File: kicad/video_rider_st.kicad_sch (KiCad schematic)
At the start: 32 parts, among them J1 F3311A7H121020E200, J2 F3311A7H121020E200, J3 Conn_01x02_Male, J4 Conn_01x03_Male, J5 F3311A7H121020E200, J6 F3311A7H121020E200, J7 Conn_01x06_Male, U1 ST_SHIFTER_PHY, U10 ST_GLUE_SOCKET, U2 ST_SHIFTER_SOCKET, U3 Pico, U4 74HC245, U5 74HC245, U6 74HC245, U7 74HC245, U8 XC95144XL-TQ100, U9 ST_GLUE_PHY, X1 CXO_DIP14

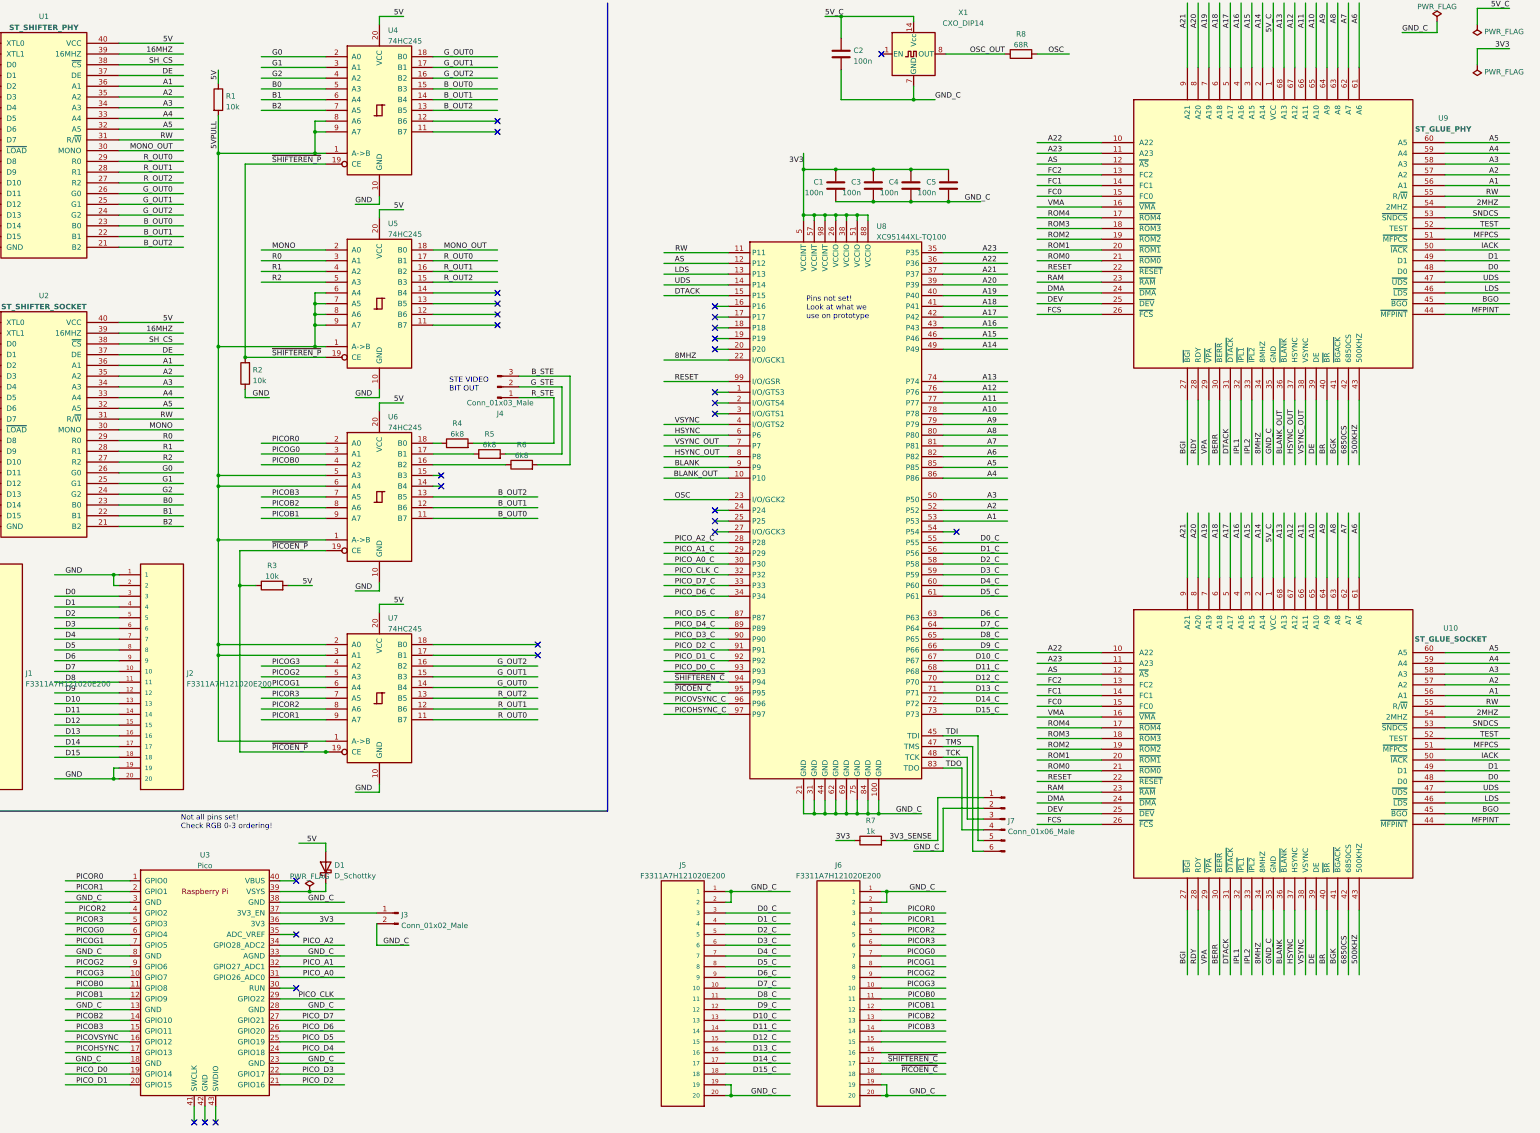
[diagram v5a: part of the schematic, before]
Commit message: Basic board outline and routeing done. Need sanity and DRC check
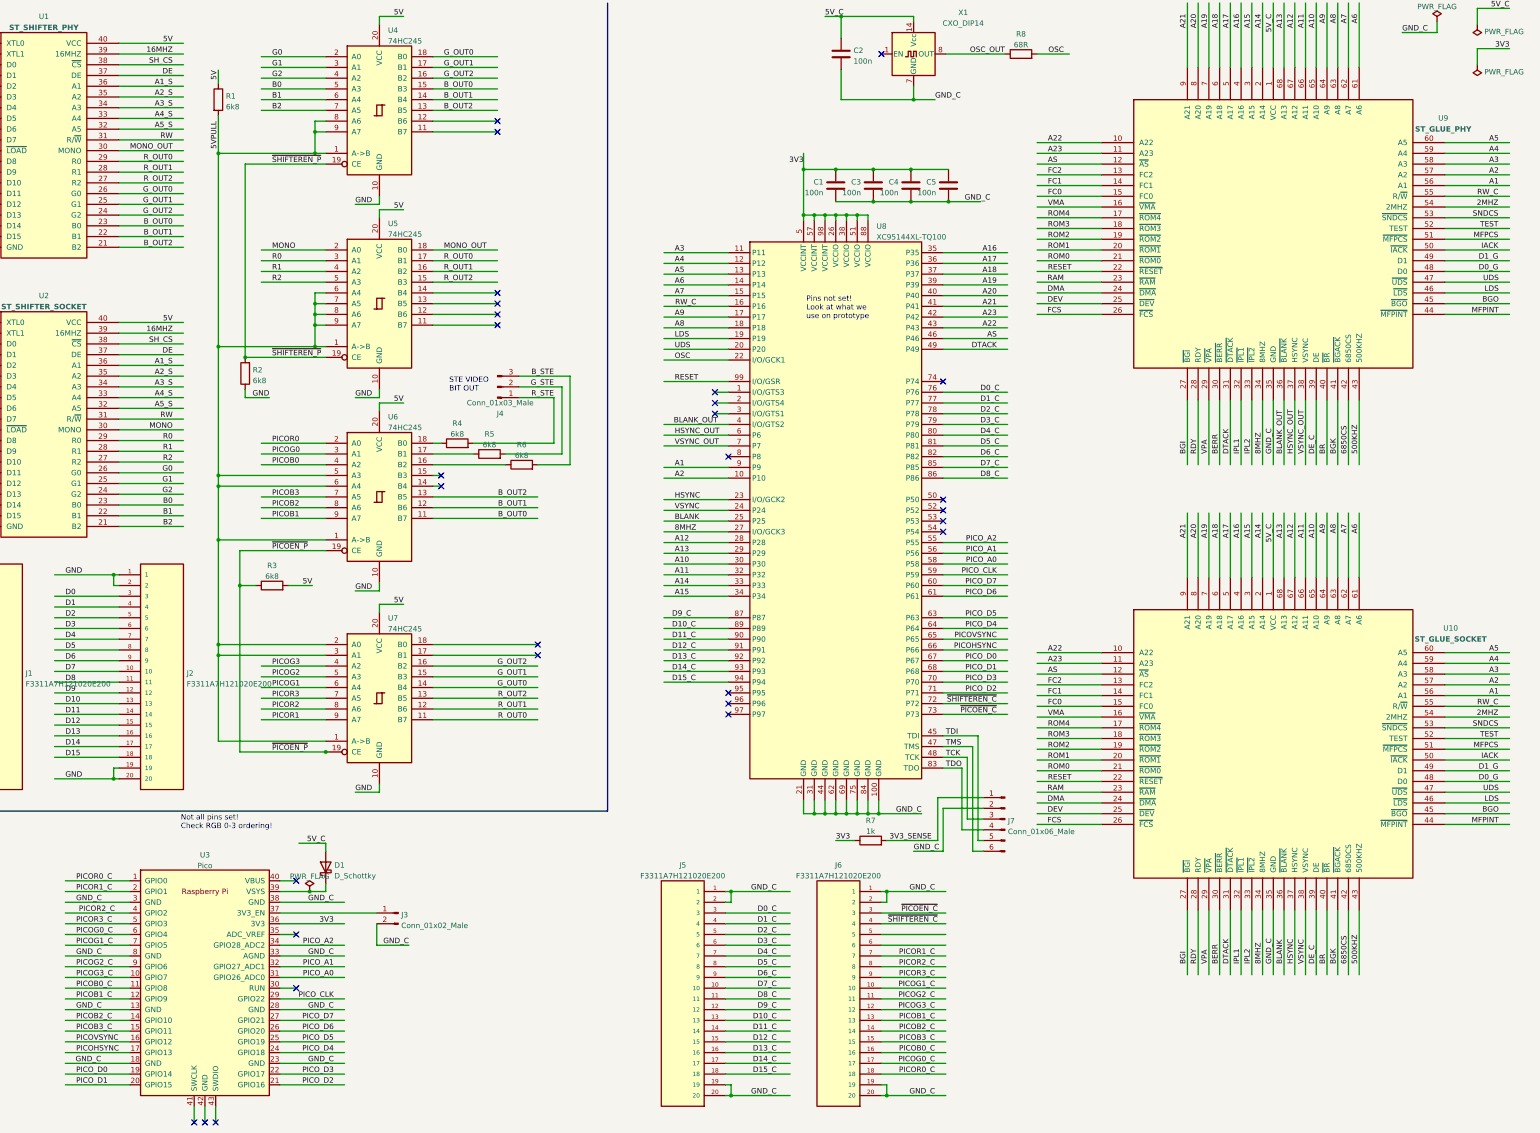
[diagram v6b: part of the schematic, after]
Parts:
- J3: footprint Connector_PinHeader_2.54mm:PinHeader_1x02_P2.54mm_Vertical -> Connector_PinHeader_2.54mm:PinHeader_1x02_P2.54mm_Horizontal
- J4: footprint Connector_PinHeader_2.54mm:PinHeader_1x03_P2.54mm_Horizontal -> Connector_PinHeader_2.54mm:PinHeader_1x03_P2.54mm_Vertical
- J7: footprint Connector_PinHeader_2.54mm:PinHeader_1x06_P2.54mm_Horizontal -> Connector_PinHeader_2.54mm:PinHeader_1x06_P2.54mm_Vertical
- R1, R2, R3: value 10k -> 6k8
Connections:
- net PICO_A0_C is gone; now on net A10: U8.30 (P30)
- net PICO_A1_C is gone; now on net A13: U8.29 (P29)
- net PICO_A2_C is gone; now on net A12: U8.28 (P28)
- net PICO_CLK_C is gone; now on net A11: U8.32 (P32)
- net PICO_D0_C is gone; now on net D14_C: U8.93 (P93)
- net PICO_D1_C is gone; now on net D13_C: U8.92 (P92)
- net PICO_D2_C is gone; now on net D12_C: U8.91 (P91)
- net PICO_D3_C is gone; now on net D11_C: U8.90 (P90)
- net PICO_D4_C is gone; now on net D10_C: U8.89 (P89)
- net PICO_D5_C is gone; now on net D9_C: U8.87 (P87)
- net PICO_D6_C is gone; now on net A15: U8.34 (P34)
- net PICO_D7_C is gone; now on net A14: U8.33 (P33)
- net 5V: no longer D1.2 (A)
- net 5V_C: now also D1.2 (A)
- net 8MHZ: now also U8.27 (I/O/GCK3); no longer U8.22 (I/O/GCK1)
- net A1: now also U8.9 (P9); no longer U1.36 (A1), U2.36 (A1), U8.53 (P53)
- net A10: no longer U8.78 (P78)
- net A11: no longer U8.77 (P77)
- net A12: no longer U8.76 (P76)
- net A13: no longer U8.74 (P74)
- net A14: no longer U8.49 (P49)
- net A15: no longer U8.46 (P46)
- net A16: now also U8.35 (P35); no longer U8.43 (P43)
- net A17: now also U8.36 (P36); no longer U8.42 (P42)
- net A18: now also U8.37 (P37); no longer U8.41 (P41)
- net A19: now also U8.39 (P39); no longer U8.40 (P40)
- net A2: now also U8.10 (P10); no longer U1.35 (A2), U2.35 (A2), U8.52 (P52)
- net A20: now also U8.40 (P40); no longer U8.39 (P39)
- net A21: now also U8.41 (P41); no longer U8.37 (P37)
- net A22: now also U8.43 (P43); no longer U8.36 (P36)
- net A23: now also U8.42 (P42); no longer U8.35 (P35)
- net A3: now also U8.11 (P11); no longer U1.34 (A3), U2.34 (A3), U8.50 (P50)
- net A4: now also U8.12 (P12); no longer U1.33 (A4), U2.33 (A4), U8.86 (P86)
- net A5: now also U8.13 (P13); no longer U1.32 (A5), U2.32 (A5), U8.85 (P85)
- net A6: now also U8.14 (P14); no longer U8.82 (P82)
- net A7: now also U8.15 (P15); no longer U8.81 (P81)
- net A8: now also U8.18 (P18); no longer U8.80 (P80)
- net A9: now also U8.17 (P17); no longer U8.79 (P79)
- net AS: now also U8.46 (P46); no longer U8.12 (P12)
- net BLANK: now also U8.25 (P25); no longer U8.9 (P9)
- net BLANK_OUT: now also U8.4 (I/O/GTS2); no longer U8.10 (P10)
- net D0: no longer U10.48 (D0), U9.48 (D0)
- net D0_C: now also U8.76 (P76); no longer U8.55 (P55)
- net D1: no longer U10.49 (D1), U9.49 (D1)
- net D10_C: no longer U8.67 (P67)
- net D11_C: no longer U8.68 (P68)
- net D12_C: no longer U8.70 (P70)
- net D13_C: no longer U8.71 (P71)
- net D14_C: no longer U8.72 (P72)
- net D15_C: now also U8.94 (P94); no longer U8.73 (P73)
- net D1_C: now also U8.77 (P77); no longer U8.56 (P56)
- net D2_C: now also U8.78 (P78); no longer U8.58 (P58)
- net D3_C: now also U8.79 (P79); no longer U8.59 (P59)
- net D4_C: now also U8.80 (P80); no longer U8.60 (P60)
- net D5_C: now also U8.81 (P81); no longer U8.61 (P61)
- net D6_C: now also U8.82 (P82); no longer U8.63 (P63)
- net D7_C: now also U8.85 (P85); no longer U8.64 (P64)
- net D8_C: now also U8.86 (P86); no longer U8.65 (P65)
- net D9_C: no longer U8.66 (P66)
- net DE: no longer U10.39 (DE), U9.39 (DE)
- net DTACK: now also U8.49 (P49); no longer U8.15 (P15)
- net HSYNC: now also U8.23 (I/O/GCK2); no longer U8.6 (P6)
- net HSYNC_OUT: now also U8.6 (P6); no longer U8.8 (P8)
- net LDS: now also U8.19 (P19); no longer U8.13 (P13)
- net OSC: now also U8.22 (I/O/GCK1); no longer U8.23 (I/O/GCK2)
- net PICOB0: no longer J6.11, U3.11 (GPIO8)
- net PICOB1: no longer J6.12, U3.12 (GPIO9)
- net PICOB2: no longer J6.13, U3.14 (GPIO10)
- net PICOB3: no longer J6.14, U3.15 (GPIO11)
- net PICOG0: no longer J6.7, U3.6 (GPIO4)
- net PICOG1: no longer J6.8, U3.7 (GPIO5)
- net PICOG2: no longer J6.9, U3.9 (GPIO6)
- net PICOG3: no longer J6.10, U3.10 (GPIO7)
- net PICOHSYNC: now also U8.66 (P66)
- net PICOR0: no longer J6.3, U3.1 (GPIO0)
- net PICOR1: no longer J6.4, U3.2 (GPIO1)
- net PICOR2: no longer J6.5, U3.4 (GPIO2)
- net PICOR3: no longer J6.6, U3.5 (GPIO3)
- net PICOVSYNC: now also U8.65 (P65)
- net PICO_A0: now also U8.58 (P58)
- net PICO_A1: now also U8.56 (P56)
- net PICO_A2: now also U8.55 (P55)
- net PICO_CLK: now also U8.59 (P59)
- net PICO_D0: now also U8.67 (P67)
- net PICO_D1: now also U8.68 (P68)
- net PICO_D2: now also U8.71 (P71)
- net PICO_D3: now also U8.70 (P70)
- net PICO_D4: now also U8.64 (P64)
- net PICO_D5: now also U8.63 (P63)
- net PICO_D6: now also U8.61 (P61)
- net PICO_D7: now also U8.60 (P60)
- net RW: no longer U10.55 (R/~{W}), U8.11 (P11), U9.55 (R/~{W})
- net UDS: now also U8.20 (P20); no longer U8.14 (P14)
- net VSYNC: now also U8.24 (P24); no longer U8.4 (I/O/GTS2)
- net ~{PICOEN_C}: now also J6.3, U8.73 (P73); no longer J6.18, U8.95 (P95)
- net ~{SHIFTEREN_C}: now also J6.4, U8.72 (P72); no longer J6.17, U8.94 (P94)
- net RW_C: now reaches U8.16 (P16)
- net RW_C: now also U10.55 (R/~{W}), U9.55 (R/~{W})
- net PICOB3_C: now reaches J6.15
- net PICOB3_C: now also U3.15 (GPIO11)
- net PICOB0_C: now reaches J6.16
- net PICOB0_C: now also U3.11 (GPIO8)
- net PICOHSYNC_C: no longer names the net of U8.97 (P97)
- net PICOVSYNC_C: no longer names the net of U8.96 (P96)
- new net A1_S: U1.36 (A1), U2.36 (A1)
- new net A2_S: U1.35 (A2), U2.35 (A2)
- new net A3_S: U1.34 (A3), U2.34 (A3)
- new net A4_S: U1.33 (A4), U2.33 (A4)
- new net A5_S: U1.32 (A5), U2.32 (A5)
- new net D0_G: U10.48 (D0), U9.48 (D0)
- new net D1_G: U10.49 (D1), U9.49 (D1)
- new net DE_C: U10.39 (DE), U9.39 (DE)
- new net PICOB1_C: J6.13, U3.12 (GPIO9)
- new net PICOB2_C: J6.14, U3.14 (GPIO10)
- new net PICOG0_C: J6.17, U3.6 (GPIO4)
- new net PICOG1_C: J6.10, U3.7 (GPIO5)
- new net PICOG2_C: J6.11, U3.9 (GPIO6)
- new net PICOG3_C: J6.12, U3.10 (GPIO7)
- new net PICOR0_C: J6.18, U3.1 (GPIO0)
- new net PICOR1_C: J6.7, U3.2 (GPIO1)
- new net PICOR2_C: J6.8, U3.4 (GPIO2)
- new net PICOR3_C: J6.9, U3.5 (GPIO3)

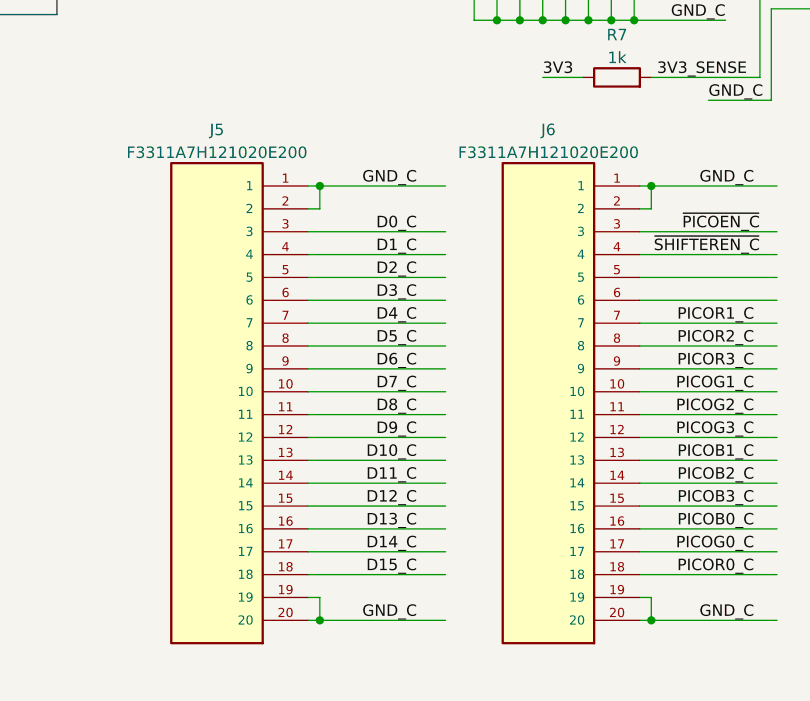
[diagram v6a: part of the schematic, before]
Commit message: Rerouteing pico to bottom layer
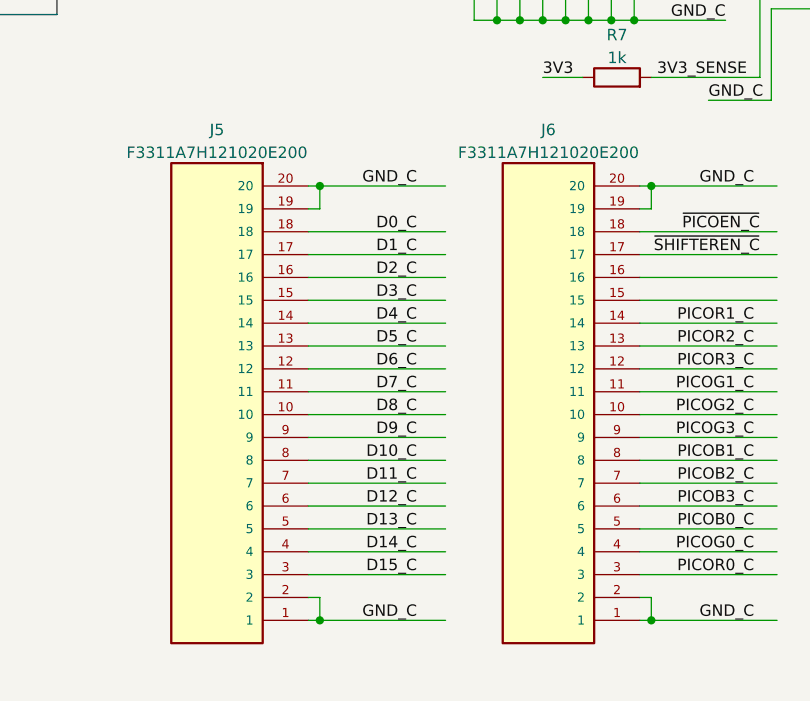
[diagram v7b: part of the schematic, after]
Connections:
- net D0_C: now also J5.18; no longer J5.3
- net D10_C: now also J5.8; no longer J5.13
- net D11_C: now also J5.7; no longer J5.14
- net D12_C: now also J5.6; no longer J5.15
- net D13_C: now also J5.5; no longer J5.16
- net D14_C: now also J5.4; no longer J5.17
- net D15_C: now also J5.3; no longer J5.18
- net D1_C: now also J5.17; no longer J5.4
- net D2_C: now also J5.16; no longer J5.5
- net D3_C: now also J5.15; no longer J5.6
- net D4_C: now also J5.14; no longer J5.7
- net D5_C: now also J5.13; no longer J5.8
- net D6_C: now also J5.12; no longer J5.9
- net D7_C: now also J5.11; no longer J5.10
- net D8_C: now also J5.10; no longer J5.11
- net D9_C: now also J5.9; no longer J5.12
- net PICOB0_C: now also J6.5; no longer J6.16
- net PICOB1_C: now also J6.8; no longer J6.13
- net PICOB2_C: now also J6.7; no longer J6.14
- net PICOB3_C: now also J6.6; no longer J6.15
- net PICOG0_C: now also J6.4; no longer J6.17
- net PICOG1_C: now also J6.11; no longer J6.10
- net PICOG2_C: now also J6.10; no longer J6.11
- net PICOG3_C: now also J6.9; no longer J6.12
- net PICOR0_C: now also J6.3; no longer J6.18
- net PICOR1_C: now also J6.14; no longer J6.7
- net PICOR2_C: now also J6.13; no longer J6.8
- net PICOR3_C: now also J6.12; no longer J6.9
- net ~{PICOEN_C}: now also J6.18; no longer J6.3
- net ~{SHIFTEREN_C}: now also J6.17; no longer J6.4
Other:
- moved on the sheet: J5, J6
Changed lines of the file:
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@@
     (pin "9")
   )
-  (symbol (lib_id "F3311A7H121020E200:F3311A7H121020E200") (at 208.28 248.92 0) (mirror y) (unit 1)
+  (symbol (lib_id "F3311A7H121020E200:F3311A7H121020E200") (at 208.28 251.46 180) (unit 1)
     (in_bom yes) (on_board yes) (fields_autoplaced)
     (property "Reference" "J5" (id 0) (at 208.28 219.8202 0))
     (property "Value" "F3311A7H121020E200" (id 1) (at 208.28 222.3571 0))
-    (property "Footprint" "F3311A7H121020E200:AMPHENOL_F3311A7H121020E200" (id 2) (at 208.28 248.92 0)
-      (effects (font (size 1.27 1.27)) (justify bottom) hide)
-    )
-    (property "Datasheet" "" (id 3) (at 208.28 248.92 0)
-      (effects (font (size 1.27 1.27)) hide)
-    )
-    (property "PARTREV" "A" (id 4) (at 208.28 248.92 0)
-      (effects (font (size 1.27 1.27)) (justify bottom) hide)
-    )
-    (property "STANDARD" "Manufacturer Recommendations" (id 5) (at 208.28 248.92 0)
-      (effects (font (size 1.27 1.27)) (justify bottom) hide)
-    )
-    (property "MAXIMUM_PACKAGE_HEIGHT" "1.62 mm" (id 6) (at 208.28 248.92 0)
-      (effects (font (size 1.27 1.27)) (justify bottom) hide)
-    )
-    (property "MANUFACTURER" "Amphenol" (id 7) (at 208.28 248.92 0)
+    (property "Footprint" "F3311A7H121020E200:AMPHENOL_F3311A7H121020E200" (id 2) (at 208.28 251.46 0)
+      (effects (font (size 1.27 1.27)) (justify bottom) hide)
+    )
+    (property "Datasheet" "" (id 3) (at 208.28 251.46 0)
+      (effects (font (size 1.27 1.27)) hide)
+    )
+    (property "PARTREV" "A" (id 4) (at 208.28 251.46 0)
+      (effects (font (size 1.27 1.27)) (justify bottom) hide)
+    )
+    (property "STANDARD" "Manufacturer Recommendations" (id 5) (at 208.28 251.46 0)
+      (effects (font (size 1.27 1.27)) (justify bottom) hide)
+    )
+    (property "MAXIMUM_PACKAGE_HEIGHT" "1.62 mm" (id 6) (at 208.28 251.46 0)
+      (effects (font (size 1.27 1.27)) (justify bottom) hide)
+    )
+    (property "MANUFACTURER" "Amphenol" (id 7) (at 208.28 251.46 0)
       (effects (font (size 1.27 1.27)) (justify bottom) hide)
     )
@@
     (pin "9")
   )
-  (symbol (lib_id "F3311A7H121020E200:F3311A7H121020E200") (at 245.11 248.92 0) (mirror y) (unit 1)
+  (symbol (lib_id "F3311A7H121020E200:F3311A7H121020E200") (at 245.11 251.46 180) (unit 1)
     (in_bom yes) (on_board yes) (fields_autoplaced)
     (property "Reference" "J6" (id 0) (at 245.11 219.8202 0))
     (property "Value" "F3311A7H121020E200" (id 1) (at 245.11 222.3571 0))
-    (property "Footprint" "F3311A7H121020E200:AMPHENOL_F3311A7H121020E200" (id 2) (at 245.11 248.92 0)
-      (effects (font (size 1.27 1.27)) (justify bottom) hide)
-    )
-    (property "Datasheet" "" (id 3) (at 245.11 248.92 0)
-      (effects (font (size 1.27 1.27)) hide)
-    )
-    (property "PARTREV" "A" (id 4) (at 245.11 248.92 0)
-      (effects (font (size 1.27 1.27)) (justify bottom) hide)
-    )
-    (property "STANDARD" "Manufacturer Recommendations" (id 5) (at 245.11 248.92 0)
-      (effects (font (size 1.27 1.27)) (justify bottom) hide)
-    )
-    (property "MAXIMUM_PACKAGE_HEIGHT" "1.62 mm" (id 6) (at 245.11 248.92 0)
-      (effects (font (size 1.27 1.27)) (justify bottom) hide)
-    )
-    (property "MANUFACTURER" "Amphenol" (id 7) (at 245.11 248.92 0)
-      (effects (font (size 1.27 1.27)) (justify bottom) hide)
-    )
+    (property "Footprint" "F3311A7H121020E200:AMPHENOL_F3311A7H121020E200" (id 2) (at 245.11 251.46 0)
+      (effects (font (size 1.27 1.27)) (justify bottom) hide)
+    )
+    (property "Datasheet" "" (id 3) (at 245.11 251.46 0)
+      (effects (font (size 1.27 1.27)) hide)
+    )
+    (property "PARTREV" "A" (id 4) (at 245.11 251.46 0)
+      (effects (font (size 1.27 1.27)) (justify bottom) hide)
+    )
+    (property "STANDARD" "Manufacturer Recommendations" (id 5) (at 245.11 251.46 0)
+      (effects (font (size 1.27 1.27)) (justify bottom) hide)
+    )
+    (property "MAXIMUM_PACKAGE_HEIGHT" "1.62 mm" (id 6) (at 245.11 251.46 0)
+      (effects (font (size 1.27 1.27)) (justify bottom) hide)
+    )
+    (property "MANUFACTURER" "Amphenol" (id 7) (at 245.11 251.46 0)
+      (effects (font (size 1.27 1.27)) (justify bottom) hide)
+    )
